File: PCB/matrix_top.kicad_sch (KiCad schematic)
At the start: 56 parts, among them J21 Conn_02x02_Top_Bottom, J22 Conn_02x02_Top_Bottom, J23 Conn_02x02_Top_Bottom, J24 Conn_02x02_Top_Bottom, J26 Conn_01x04, J28 Conn_01x04

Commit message: ピンヘッダのピン順を変更。フットプリント割り当て。
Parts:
- EXT_C16, EXT_C17, EXT_C18, EXT_C19, EXT_C20, EXT_C21, EXT_C22, EXT_C23, EXT_R20, EXT_R21, EXT_R22, EXT_R23: footprint TestPoint:TestPoint_THTPad_D1.5mm_Drill0.7mm -> TestPoint:TestPoint_THTPad_D2.0mm_Drill1.0mm
- J21, J22, J23, J24: footprint (none) -> Connector_PinHeader_2.54mm:PinHeader_2x02_P2.54mm_Vertical; symbol Connector_Generic:Conn_02x02_Top_Bottom -> Connector_Generic:Conn_02x02_Odd_Even
- J26, J28: footprint (none) -> Connector_PinHeader_2.54mm:PinHeader_1x04_P2.54mm_Vertical
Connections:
- net Top_col0: now also J21.2 (Pin_2); no longer J21.3 (Pin_3)
- net Top_col1: now also J22.3 (Pin_3); no longer J22.2 (Pin_2)
- net Top_col2: now also J22.2 (Pin_2); no longer J22.3 (Pin_3)
- net Top_col5: now also J23.3 (Pin_3); no longer J23.2 (Pin_2)
- net Top_col6: now also J23.2 (Pin_2), J24.2 (Pin_2); no longer J23.3 (Pin_3), J24.3 (Pin_3)
- net Top_row5: now also J21.3 (Pin_3), J24.3 (Pin_3); no longer J21.2 (Pin_2), J24.2 (Pin_2)
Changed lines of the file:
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@@
     (pin "2")
   )
-  (symbol (lib_id "Connector_Generic:Conn_02x02_Top_Bottom") (at 90.805 132.08 0) (unit 1)
+  (symbol (lib_id "Connector_Generic:Conn_02x02_Odd_Even") (at 90.805 132.08 0) (unit 1)
     (in_bom yes) (on_board yes) (fields_autoplaced)
     (property "Reference" "J22" (id 0) (at 92.075 127.1102 0))
     (property "Value" "Conn_02x02_Top_Bottom" (id 1) (at 92.075 129.6471 0))
-    (property "Footprint" "" (id 2) (at 90.805 132.08 0)
+    (property "Footprint" "Connector_PinHeader_2.54mm:PinHeader_2x02_P2.54mm_Vertical" (id 2) (at 90.805 132.08 0)
       (effects (font (size 1.27 1.27)) hide)
     )
@@
       (effects (font (size 1.27 1.27)) (justify left))
     )
-    (property "Footprint" "TestPoint:TestPoint_THTPad_D1.5mm_Drill0.7mm" (id 2) (at 284.48 101.6 0)
+    (property "Footprint" "TestPoint:TestPoint_THTPad_D2.0mm_Drill1.0mm" (id 2) (at 284.48 101.6 0)
       (effects (font (size 1.27 1.27)) hide)
     )
@@
       (effects (font (size 1.27 1.27)) (justify left))
     )
-    (property "Footprint" "TestPoint:TestPoint_THTPad_D1.5mm_Drill0.7mm" (id 2) (at 170.18 110.49 0)
+    (property "Footprint" "TestPoint:TestPoint_THTPad_D2.0mm_Drill1.0mm" (id 2) (at 170.18 110.49 0)
       (effects (font (size 1.27 1.27)) hide)
     )
@@
       (effects (font (size 1.27 1.27)) (justify left))
     )
-    (property "Footprint" "TestPoint:TestPoint_THTPad_D1.5mm_Drill0.7mm" (id 2) (at 137.16 110.49 0)
+    (property "Footprint" "TestPoint:TestPoint_THTPad_D2.0mm_Drill1.0mm" (id 2) (at 137.16 110.49 0)
       (effects (font (size 1.27 1.27)) hide)
     )
@@
       (effects (font (size 1.27 1.27)) (justify left))
     )
-    (property "Footprint" "TestPoint:TestPoint_THTPad_D1.5mm_Drill0.7mm" (id 2) (at 203.2 110.49 0)
+    (property "Footprint" "TestPoint:TestPoint_THTPad_D2.0mm_Drill1.0mm" (id 2) (at 203.2 110.49 0)
       (effects (font (size 1.27 1.27)) hide)
     )
@@
     (property "Reference" "J28" (id 0) (at 139.7 142.3502 0))
     (property "Value" "Conn_01x04" (id 1) (at 139.7 144.8871 0))
-    (property "Footprint" "" (id 2) (at 139.7 149.86 0)
+    (property "Footprint" "Connector_PinHeader_2.54mm:PinHeader_1x04_P2.54mm_Vertical" (id 2) (at 139.7 149.86 0)
       (effects (font (size 1.27 1.27)) hide)
     )
@@
     (pin "2")
   )
-  (symbol (lib_id "Connector_Generic:Conn_02x02_Top_Bottom") (at 40.005 132.08 0) (unit 1)
+  (symbol (lib_id "Connector_Generic:Conn_02x02_Odd_Even") (at 40.005 132.08 0) (unit 1)
     (in_bom yes) (on_board yes) (fields_autoplaced)
     (property "Reference" "J21" (id 0) (at 41.275 127.1102 0))
     (property "Value" "Conn_02x02_Top_Bottom" (id 1) (at 41.275 129.6471 0))
-    (property "Footprint" "" (id 2) (at 40.005 132.08 0)
+    (property "Footprint" "Connector_PinHeader_2.54mm:PinHeader_2x02_P2.54mm_Vertical" (id 2) (at 40.005 132.08 0)
       (effects (font (size 1.27 1.27)) hide)
     )
@@
       (effects (font (size 1.27 1.27)) (justify left))
     )
-    (property "Footprint" "TestPoint:TestPoint_THTPad_D1.5mm_Drill0.7mm" (id 2) (at 236.22 110.49 0)
+    (property "Footprint" "TestPoint:TestPoint_THTPad_D2.0mm_Drill1.0mm" (id 2) (at 236.22 110.49 0)
       (effects (font (size 1.27 1.27)) hide)
     )
@@
       (effects (font (size 1.27 1.27)) (justify left))
     )
-    (property "Footprint" "TestPoint:TestPoint_THTPad_D1.5mm_Drill0.7mm" (id 2) (at 269.24 110.49 0)
+    (property "Footprint" "TestPoint:TestPoint_THTPad_D2.0mm_Drill1.0mm" (id 2) (at 269.24 110.49 0)
       (effects (font (size 1.27 1.27)) hide)
     )
@@
     (pin "1")
   )
-  (symbol (lib_id "Connector_Generic:Conn_02x02_Top_Bottom") (at 192.405 132.08 0) (unit 1)
+  (symbol (lib_id "Connector_Generic:Conn_02x02_Odd_Even") (at 192.405 132.08 0) (unit 1)
     (in_bom yes) (on_board yes) (fields_autoplaced)
     (property "Reference" "J24" (id 0) (at 193.675 127.1102 0))
     (property "Value" "Conn_02x02_Top_Bottom" (id 1) (at 193.675 129.6471 0))
-    (property "Footprint" "" (id 2) (at 192.405 132.08 0)
+    (property "Footprint" "Connector_PinHeader_2.54mm:PinHeader_2x02_P2.54mm_Vertical" (id 2) (at 192.405 132.08 0)
       (effects (font (size 1.27 1.27)) hide)
     )
@@
       (effects (font (size 1.27 1.27)) (justify left))
     )
-    (property "Footprint" "TestPoint:TestPoint_THTPad_D1.5mm_Drill0.7mm" (id 2) (at 284.48 99.06 0)
+    (property "Footprint" "TestPoint:TestPoint_THTPad_D2.0mm_Drill1.0mm" (id 2) (at 284.48 99.06 0)
       (effects (font (size 1.27 1.27)) hide)
     )
@@
       (effects (font (size 1.27 1.27)) (justify left))
     )
-    (property "Footprint" "TestPoint:TestPoint_THTPad_D1.5mm_Drill0.7mm" (id 2) (at 104.14 110.49 0)
+    (property "Footprint" "TestPoint:TestPoint_THTPad_D2.0mm_Drill1.0mm" (id 2) (at 104.14 110.49 0)
       (effects (font (size 1.27 1.27)) hide)
     )
@@
       (effects (font (size 1.27 1.27)) (justify left))
     )
-    (property "Footprint" "TestPoint:TestPoint_THTPad_D1.5mm_Drill0.7mm" (id 2) (at 284.48 67.31 0)
+    (property "Footprint" "TestPoint:TestPoint_THTPad_D2.0mm_Drill1.0mm" (id 2) (at 284.48 67.31 0)
       (effects (font (size 1.27 1.27)) hide)
     )
@@
       (effects (font (size 1.27 1.27)) (justify left))
     )
-    (property "Footprint" "TestPoint:TestPoint_THTPad_D1.5mm_Drill0.7mm" (id 2) (at 284.48 69.85 0)
+    (property "Footprint" "TestPoint:TestPoint_THTPad_D2.0mm_Drill1.0mm" (id 2) (at 284.48 69.85 0)
       (effects (font (size 1.27 1.27)) hide)
     )
@@
     (pin "2")
   )
-  (symbol (lib_id "Connector_Generic:Conn_02x02_Top_Bottom") (at 141.605 132.08 0) (unit 1)
+  (symbol (lib_id "Connector_Generic:Conn_02x02_Odd_Even") (at 141.605 132.08 0) (unit 1)
     (in_bom yes) (on_board yes) (fields_autoplaced)
     (property "Reference" "J23" (id 0) (at 142.875 127.1102 0))
     (property "Value" "Conn_02x02_Top_Bottom" (id 1) (at 142.875 129.6471 0))
-    (property "Footprint" "" (id 2) (at 141.605 132.08 0)
+    (property "Footprint" "Connector_PinHeader_2.54mm:PinHeader_2x02_P2.54mm_Vertical" (id 2) (at 141.605 132.08 0)
       (effects (font (size 1.27 1.27)) hide)
     )
@@
       (effects (font (size 1.27 1.27)) (justify left))
     )
-    (property "Footprint" "TestPoint:TestPoint_THTPad_D1.5mm_Drill0.7mm" (id 2) (at 38.1 110.49 0)
+    (property "Footprint" "TestPoint:TestPoint_THTPad_D2.0mm_Drill1.0mm" (id 2) (at 38.1 110.49 0)
       (effects (font (size 1.27 1.27)) hide)
     )
@@
       (effects (font (size 1.27 1.27)) (justify left))
     )
-    (property "Footprint" "TestPoint:TestPoint_THTPad_D1.5mm_Drill0.7mm" (id 2) (at 71.12 110.49 0)
+    (property "Footprint" "TestPoint:TestPoint_THTPad_D2.0mm_Drill1.0mm" (id 2) (at 71.12 110.49 0)
       (effects (font (size 1.27 1.27)) hide)
     )
@@
     (property "Reference" "J26" (id 0) (at 88.9 142.3502 0))
     (property "Value" "Conn_01x04" (id 1) (at 88.9 144.8871 0))
-    (property "Footprint" "" (id 2) (at 88.9 149.86 0)
-      (effects (font (size 1.27 1.27)) hide)
-    )
+    (property "Footprint" "Connector_PinHeader_2.54mm:PinHeader_1x04_P2.54mm_Vertical" (id 2) (at 88.9 149.86 0)
+      (effects (font (size 1.27 1.27)) hide)
+    )

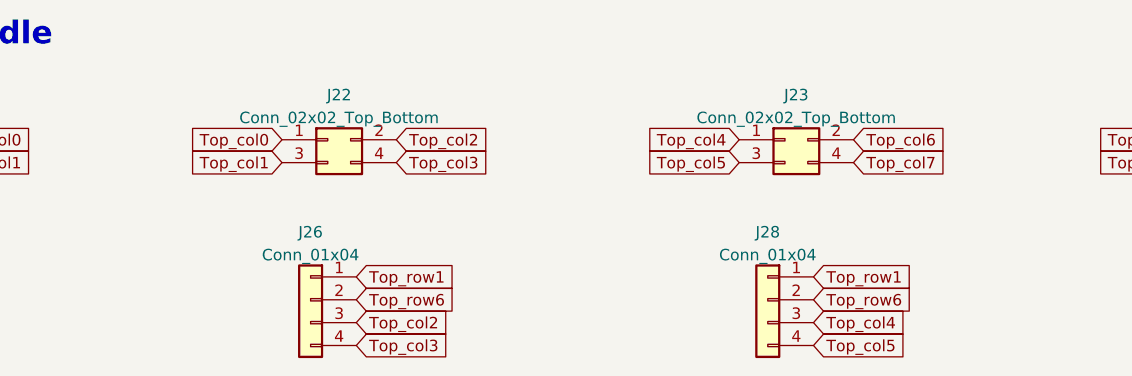
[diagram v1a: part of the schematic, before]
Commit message: 子基板仮配置。コネクタ形状、位置を変更。
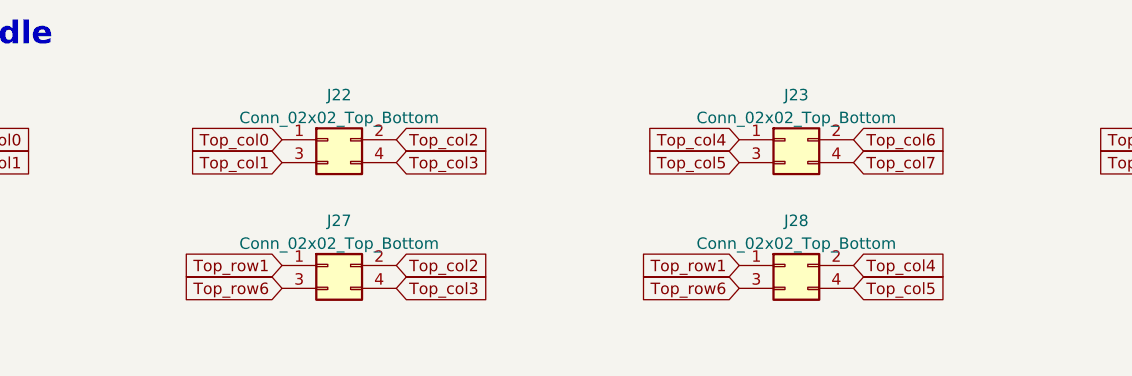
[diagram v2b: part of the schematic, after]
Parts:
- removed J26, J28: Conn_01x04, Connector_PinHeader_2.54mm:PinHeader_1x04_P2.54mm_Vertical, symbol Connector_Generic:Conn_01x04
- added J27, J28: Conn_02x02_Top_Bottom, Connector_PinHeader_2.54mm:PinHeader_2x02_P2.54mm_Vertical, symbol Connector_Generic:Conn_02x02_Odd_Even
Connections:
- net Top_col2: now also J27.2 (Pin_2)
- net Top_col3: now also J27.4 (Pin_4)
- net Top_col4: now also J28.2 (Pin_2)
- net Top_col5: now also J28.4 (Pin_4)
- net Top_row1: now also J27.1 (Pin_1), J28.1 (Pin_1)
- net Top_row6: now also J27.3 (Pin_3), J28.3 (Pin_3)
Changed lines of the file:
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@@
     )
   )
-  (global_label "Top_row6" (shape input) (at 144.78 149.86 0) (fields_autoplaced)
-    (effects (font (size 1.27 1.27)) (justify left))
-    (property "シート間のリファレンス" "${INTERSHEET_REFS}" (id 0) (at 155.8128 149.7806 0)
-      (effects (font (size 1.27 1.27)) (justify left) hide)
+  (global_label "Top_row6" (shape input) (at 136.525 148.59 180) (fields_autoplaced)
+    (effects (font (size 1.27 1.27)) (justify right))
+    (property "シート間のリファレンス" "${INTERSHEET_REFS}" (id 0) (at 125.4922 148.5106 0)
+      (effects (font (size 1.27 1.27)) (justify right) hide)
     )
   )
@@
     )
   )
-  (global_label "Top_row1" (shape input) (at 144.78 147.32 0) (fields_autoplaced)
-    (effects (font (size 1.27 1.27)) (justify left))
-    (property "シート間のリファレンス" "${INTERSHEET_REFS}" (id 0) (at 155.8128 147.2406 0)
-      (effects (font (size 1.27 1.27)) (justify left) hide)
+  (global_label "Top_row1" (shape input) (at 136.525 146.05 180) (fields_autoplaced)
+    (effects (font (size 1.27 1.27)) (justify right))
+    (property "シート間のリファレンス" "${INTERSHEET_REFS}" (id 0) (at 125.4922 145.9706 0)
+      (effects (font (size 1.27 1.27)) (justify right) hide)
     )
   )
@@
     )
   )
-  (global_label "Top_col2" (shape input) (at 93.98 152.4 0) (fields_autoplaced)
-    (effects (font (size 1.27 1.27)) (justify left))
-    (property "シート間のリファレンス" "${INTERSHEET_REFS}" (id 0) (at 104.6499 152.3206 0)
+  (global_label "Top_col2" (shape input) (at 98.425 146.05 0) (fields_autoplaced)
+    (effects (font (size 1.27 1.27)) (justify left))
+    (property "シート間のリファレンス" "${INTERSHEET_REFS}" (id 0) (at 109.0949 145.9706 0)
       (effects (font (size 1.27 1.27)) (justify left) hide)
     )
@@
     )
   )
-  (global_label "Top_col4" (shape input) (at 144.78 152.4 0) (fields_autoplaced)
-    (effects (font (size 1.27 1.27)) (justify left))
-    (property "シート間のリファレンス" "${INTERSHEET_REFS}" (id 0) (at 155.4499 152.3206 0)
+  (global_label "Top_col4" (shape input) (at 149.225 146.05 0) (fields_autoplaced)
+    (effects (font (size 1.27 1.27)) (justify left))
+    (property "シート間のリファレンス" "${INTERSHEET_REFS}" (id 0) (at 159.8949 145.9706 0)
       (effects (font (size 1.27 1.27)) (justify left) hide)
     )
@@
     )
   )
-  (global_label "Top_row6" (shape input) (at 93.98 149.86 0) (fields_autoplaced)
-    (effects (font (size 1.27 1.27)) (justify left))
-    (property "シート間のリファレンス" "${INTERSHEET_REFS}" (id 0) (at 105.0128 149.7806 0)
-      (effects (font (size 1.27 1.27)) (justify left) hide)
+  (global_label "Top_row6" (shape input) (at 85.725 148.59 180) (fields_autoplaced)
+    (effects (font (size 1.27 1.27)) (justify right))
+    (property "シート間のリファレンス" "${INTERSHEET_REFS}" (id 0) (at 74.6922 148.5106 0)
+      (effects (font (size 1.27 1.27)) (justify right) hide)
     )
   )
@@
     )
   )
-  (global_label "Top_col5" (shape input) (at 144.78 154.94 0) (fields_autoplaced)
-    (effects (font (size 1.27 1.27)) (justify left))
-    (property "シート間のリファレンス" "${INTERSHEET_REFS}" (id 0) (at 155.4499 154.8606 0)
+  (global_label "Top_col5" (shape input) (at 149.225 148.59 0) (fields_autoplaced)
+    (effects (font (size 1.27 1.27)) (justify left))
+    (property "シート間のリファレンス" "${INTERSHEET_REFS}" (id 0) (at 159.8949 148.5106 0)
       (effects (font (size 1.27 1.27)) (justify left) hide)
     )
@@
     )
   )
-  (global_label "Top_row1" (shape input) (at 93.98 147.32 0) (fields_autoplaced)
-    (effects (font (size 1.27 1.27)) (justify left))
-    (property "シート間のリファレンス" "${INTERSHEET_REFS}" (id 0) (at 105.0128 147.2406 0)
-      (effects (font (size 1.27 1.27)) (justify left) hide)
+  (global_label "Top_row1" (shape input) (at 85.725 146.05 180) (fields_autoplaced)
+    (effects (font (size 1.27 1.27)) (justify right))
+    (property "シート間のリファレンス" "${INTERSHEET_REFS}" (id 0) (at 74.6922 145.9706 0)
+      (effects (font (size 1.27 1.27)) (justify right) hide)
     )
   )
@@
     )
   )
-  (global_label "Top_col3" (shape input) (at 93.98 154.94 0) (fields_autoplaced)
-    (effects (font (size 1.27 1.27)) (justify left))
-    (property "シート間のリファレンス" "${INTERSHEET_REFS}" (id 0) (at 104.6499 154.8606 0)
+  (global_label "Top_col3" (shape input) (at 98.425 148.59 0) (fields_autoplaced)
+    (effects (font (size 1.27 1.27)) (justify left))
+    (property "シート間のリファレンス" "${INTERSHEET_REFS}" (id 0) (at 109.0949 148.5106 0)
       (effects (font (size 1.27 1.27)) (justify left) hide)
     )
@@
     (pin "1")
   )
-  (symbol (lib_id "Connector_Generic:Conn_01x04") (at 139.7 149.86 0) (mirror y) (unit 1)
+  (symbol (lib_id "Connector_Generic:Conn_02x02_Odd_Even") (at 90.805 146.05 0) (unit 1)
     (in_bom yes) (on_board yes) (fields_autoplaced)
-    (property "Reference" "J28" (id 0) (at 139.7 142.3502 0))
-    (property "Value" "Conn_01x04" (id 1) (at 139.7 144.8871 0))
-    (property "Footprint" "Connector_PinHeader_2.54mm:PinHeader_1x04_P2.54mm_Vertical" (id 2) (at 139.7 149.86 0)
-      (effects (font (size 1.27 1.27)) hide)
-    )
-    (property "Datasheet" "~" (id 3) (at 139.7 149.86 0)
+    (property "Reference" "J27" (id 0) (at 92.075 141.0802 0))
+    (property "Value" "Conn_02x02_Top_Bottom" (id 1) (at 92.075 143.6171 0))
+    (property "Footprint" "Connector_PinHeader_2.54mm:PinHeader_2x02_P2.54mm_Vertical" (id 2) (at 90.805 146.05 0)
+      (effects (font (size 1.27 1.27)) hide)
+    )
+    (property "Datasheet" "~" (id 3) (at 90.805 146.05 0)
+      (effects (font (size 1.27 1.27)) hide)
+    )
+    (pin "1")
+    (pin "2")
+    (pin "3")
+    (pin "4")
+  )
+  (symbol (lib_id "Connector_Generic:Conn_02x02_Odd_Even") (at 141.605 146.05 0) (unit 1)
+    (in_bom yes) (on_board yes) (fields_autoplaced)
+    (property "Reference" "J28" (id 0) (at 142.875 141.0802 0))
+    (property "Value" "Conn_02x02_Top_Bottom" (id 1) (at 142.875 143.6171 0))
+    (property "Footprint" "Connector_PinHeader_2.54mm:PinHeader_2x02_P2.54mm_Vertical" (id 2) (at 141.605 146.05 0)
+      (effects (font (size 1.27 1.27)) hide)
+    )
+    (property "Datasheet" "~" (id 3) (at 141.605 146.05 0)
       (effects (font (size 1.27 1.27)) hide)
     )
@@
     (pin "2")
   )
-  (symbol (lib_id "Connector_Generic:Conn_01x04") (at 88.9 149.86 0) (mirror y) (unit 1)
-    (in_bom yes) (on_board yes) (fields_autoplaced)
-    (property "Reference" "J26" (id 0) (at 88.9 142.3502 0))
-    (property "Value" "Conn_01x04" (id 1) (at 88.9 144.8871 0))
-    (property "Footprint" "Connector_PinHeader_2.54mm:PinHeader_1x04_P2.54mm_Vertical" (id 2) (at 88.9 149.86 0)
-      (effects (font (size 1.27 1.27)) hide)
-    )
-    (property "Datasheet" "~" (id 3) (at 88.9 149.86 0)
-      (effects (font (size 1.27 1.27)) hide)
-    )
-    (pin "1")
-    (pin "2")
-    (pin "3")
-    (pin "4")
-  )
   (symbol (lib_id "Device:D") (at 196.85 62.23 90) (unit 1)

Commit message: キースイッチを配置
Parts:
- J21, J22, J23, J24, J27, J28: footprint Connector_PinHeader_2.54mm:PinHeader_2x02_P2.54mm_Vertical -> Connector_PinHeader_2.00mm:PinHeader_2x02_P2.00mm_Vertical
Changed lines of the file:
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@@
     (property "Reference" "J22" (id 0) (at 92.075 127.1102 0))
     (property "Value" "Conn_02x02_Top_Bottom" (id 1) (at 92.075 129.6471 0))
-    (property "Footprint" "Connector_PinHeader_2.54mm:PinHeader_2x02_P2.54mm_Vertical" (id 2) (at 90.805 132.08 0)
+    (property "Footprint" "Connector_PinHeader_2.00mm:PinHeader_2x02_P2.00mm_Vertical" (id 2) (at 90.805 132.08 0)
       (effects (font (size 1.27 1.27)) hide)
     )
@@
     (property "Reference" "J27" (id 0) (at 92.075 141.0802 0))
     (property "Value" "Conn_02x02_Top_Bottom" (id 1) (at 92.075 143.6171 0))
-    (property "Footprint" "Connector_PinHeader_2.54mm:PinHeader_2x02_P2.54mm_Vertical" (id 2) (at 90.805 146.05 0)
+    (property "Footprint" "Connector_PinHeader_2.00mm:PinHeader_2x02_P2.00mm_Vertical" (id 2) (at 90.805 146.05 0)
       (effects (font (size 1.27 1.27)) hide)
     )
@@
     (property "Reference" "J28" (id 0) (at 142.875 141.0802 0))
     (property "Value" "Conn_02x02_Top_Bottom" (id 1) (at 142.875 143.6171 0))
-    (property "Footprint" "Connector_PinHeader_2.54mm:PinHeader_2x02_P2.54mm_Vertical" (id 2) (at 141.605 146.05 0)
+    (property "Footprint" "Connector_PinHeader_2.00mm:PinHeader_2x02_P2.00mm_Vertical" (id 2) (at 141.605 146.05 0)
       (effects (font (size 1.27 1.27)) hide)
     )
@@
     (property "Reference" "J21" (id 0) (at 41.275 127.1102 0))
     (property "Value" "Conn_02x02_Top_Bottom" (id 1) (at 41.275 129.6471 0))
-    (property "Footprint" "Connector_PinHeader_2.54mm:PinHeader_2x02_P2.54mm_Vertical" (id 2) (at 40.005 132.08 0)
+    (property "Footprint" "Connector_PinHeader_2.00mm:PinHeader_2x02_P2.00mm_Vertical" (id 2) (at 40.005 132.08 0)
       (effects (font (size 1.27 1.27)) hide)
     )
@@
     (property "Reference" "J24" (id 0) (at 193.675 127.1102 0))
     (property "Value" "Conn_02x02_Top_Bottom" (id 1) (at 193.675 129.6471 0))
-    (property "Footprint" "Connector_PinHeader_2.54mm:PinHeader_2x02_P2.54mm_Vertical" (id 2) (at 192.405 132.08 0)
+    (property "Footprint" "Connector_PinHeader_2.00mm:PinHeader_2x02_P2.00mm_Vertical" (id 2) (at 192.405 132.08 0)
       (effects (font (size 1.27 1.27)) hide)
     )
@@
     (property "Reference" "J23" (id 0) (at 142.875 127.1102 0))
     (property "Value" "Conn_02x02_Top_Bottom" (id 1) (at 142.875 129.6471 0))
-    (property "Footprint" "Connector_PinHeader_2.54mm:PinHeader_2x02_P2.54mm_Vertical" (id 2) (at 141.605 132.08 0)
-      (effects (font (size 1.27 1.27)) hide)
-    )
+    (property "Footprint" "Connector_PinHeader_2.00mm:PinHeader_2x02_P2.00mm_Vertical" (id 2) (at 141.605 132.08 0)
+      (effects (font (size 1.27 1.27)) hide)
+    )
